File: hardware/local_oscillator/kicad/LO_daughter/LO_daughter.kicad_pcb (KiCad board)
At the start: 2 copper layers, 47.8 x 37.8 mm, 51 parts, among them J1 Conn_01x09, J2 Conn_01x09, U1 ADF5355, U2 NCR2-113+, U3 SMA-J-P-H-ST-TH1

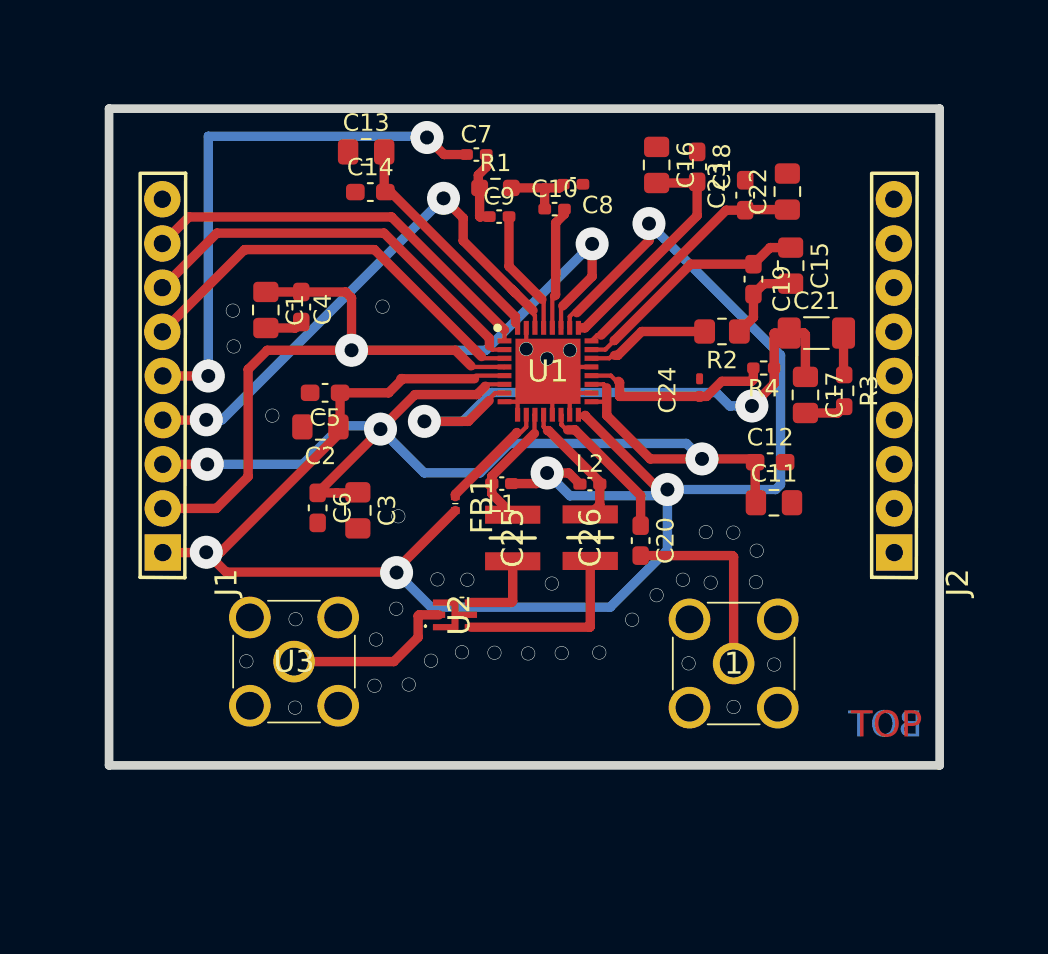
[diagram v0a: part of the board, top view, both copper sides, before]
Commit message: Update APC and LO
1) Add 30dB of fixed attenuation in feedback line of APC for better
   linearity of the power meter
2) Add power splitter for single ended outputs of the local oscillator
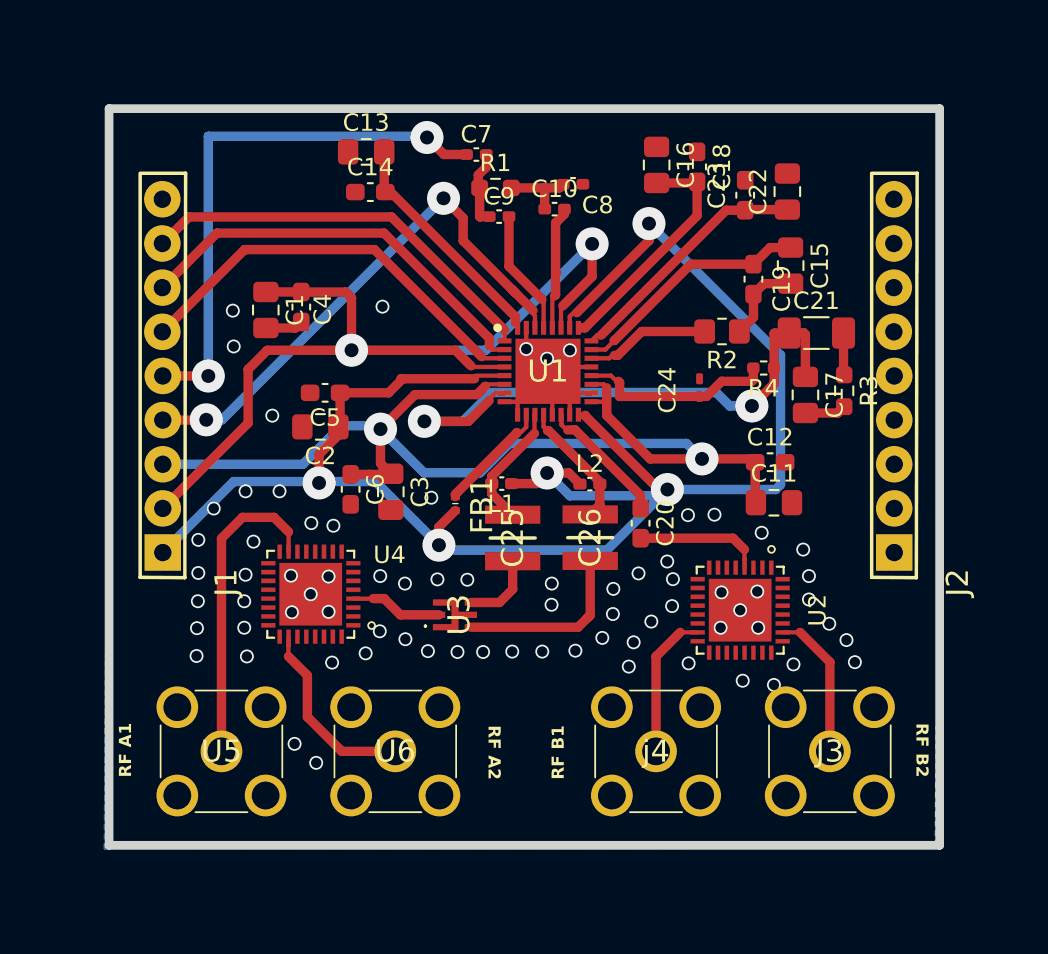
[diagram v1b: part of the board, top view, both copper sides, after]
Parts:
- added J3: SMA-J-P-H-ST-TH1, footprints:SMAJPHSTTH1, F.Cu at (171.2, 117.0)
- added U2: EP2W_, footprints:QFN51P500X500X99-33N, F.Cu at (166.0, 108.9)
- added U4: EP2W_, footprints:QFN51P500X500X99-33N, F.Cu at (141.3, 108.0)
- added U6: SMA-J-P-H-ST-TH1, footprints:SMAJPHSTTH1, F.Cu at (146.2, 117.0)
- U5: renamed from U3; footprint Connettori_sma_verticali:SMAJPHSTTH1 -> footprints:SMAJPHSTTH1
- j4: renamed from 1; footprint Connettori_sma_verticali:SMAJPHSTTH1 -> footprints:SMAJPHSTTH1
- moved j4 6.74 mm to (161.2, 117.0)
- moved U5 6.64 mm to (136.2, 117.0)
- moved C3 2.18 mm to (145.9, 102.1)
- moved C6 2.18 mm to (143.6, 102.0)
- moved C20 1.00 mm to (160.3, 103.9)
- renumbered U2 to U3
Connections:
- C2 pad 1: /3.3V_a -> GND
- C5 pad 1: /3.3V_a -> GND
- FB1 pad 1: /3.3V_a -> GND
- J1 pad 1: /3.3V_a -> GND
- L1 pad 1: /3.3V_a -> GND
- L2 pad 1: /3.3V_a -> GND
- U1 pad 16: /3.3V_a -> GND
- U1 pad 26: /3.3V_a -> GND
- U1 pad 5: /3.3V_a -> GND
- U5 pad 1: /RF_A -> /RF_A1
- j4 pad 1: /RF_B -> /RF_B1
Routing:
- net /3.3V_a: track 115.0 -> 0.00 mm, vias 5 -> 0
- net GND: track 20.7 -> 124.2 mm, vias 35 -> 79
- net /RF_A1: track 0.00 -> 18.1 mm
- net /RF_A2: track 0.00 -> 10.9 mm
- net /RF_B2: track 0.00 -> 8.56 mm
- net /RF_B1: track 0.00 -> 8.43 mm
- net /RF_A: track 10.2 -> 5.33 mm
- net /RF_B: track 11.5 -> 7.29 mm
- net /5V: track 64.9 -> 62.5 mm, vias 3 -> 2
- net /3.3V_d: track 57.4 -> 55.6 mm
- net Net-(U1-RF_OUT_B): track 8.42 -> 7.42 mm
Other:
- board size 47.8 x 37.8 mm -> 47.8 x 42.4 mm
- board text added: "RF A1"
- board text added: "RF A2"
- board text added: "RF B1"
- board text added: "RF B2"
- board text removed: "BOT"
- board text removed: "TOP"

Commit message: Generate QPCB production files
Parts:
- removed REF** (x6): n, riferimenti_pcb:aref-top
- removed REF** (x6): n, riferimenti_pcb:aref-bot
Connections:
- C2 pad 1: GND -> /3.3V_a
- C5 pad 1: GND -> /3.3V_a
- FB1 pad 1: GND -> /3.3V_a
- J1 pad 1: GND -> /3.3V_a
- L1 pad 1: GND -> /3.3V_a
- L2 pad 1: GND -> /3.3V_a
- U1 pad 16: GND -> /3.3V_a
- U1 pad 26: GND -> /3.3V_a
- U1 pad 5: GND -> /3.3V_a
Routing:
- net GND: track 124.2 -> 20.7 mm, vias 79 -> 76
- net /3.3V_a: track 0.00 -> 103.6 mm, vias 0 -> 5
- net Net-(U1-CPout): track 34.1 -> 33.4 mm
